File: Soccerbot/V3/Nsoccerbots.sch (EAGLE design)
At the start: 67 parts, among them CN2 1X4-CLEANBIG, IC1 LM340S-05, IC2 TB6612FNG, IC4 TB6612FNG, J3 1X5, J4 1X5, Q1 AOD417, SW2 SPST_TACT-EVQQ2, U1 PCA9685, X1 NXT-SOCKET, X2 NXT-SOCKET, X3 NXT-SOCKET, X4 NXT-SOCKET

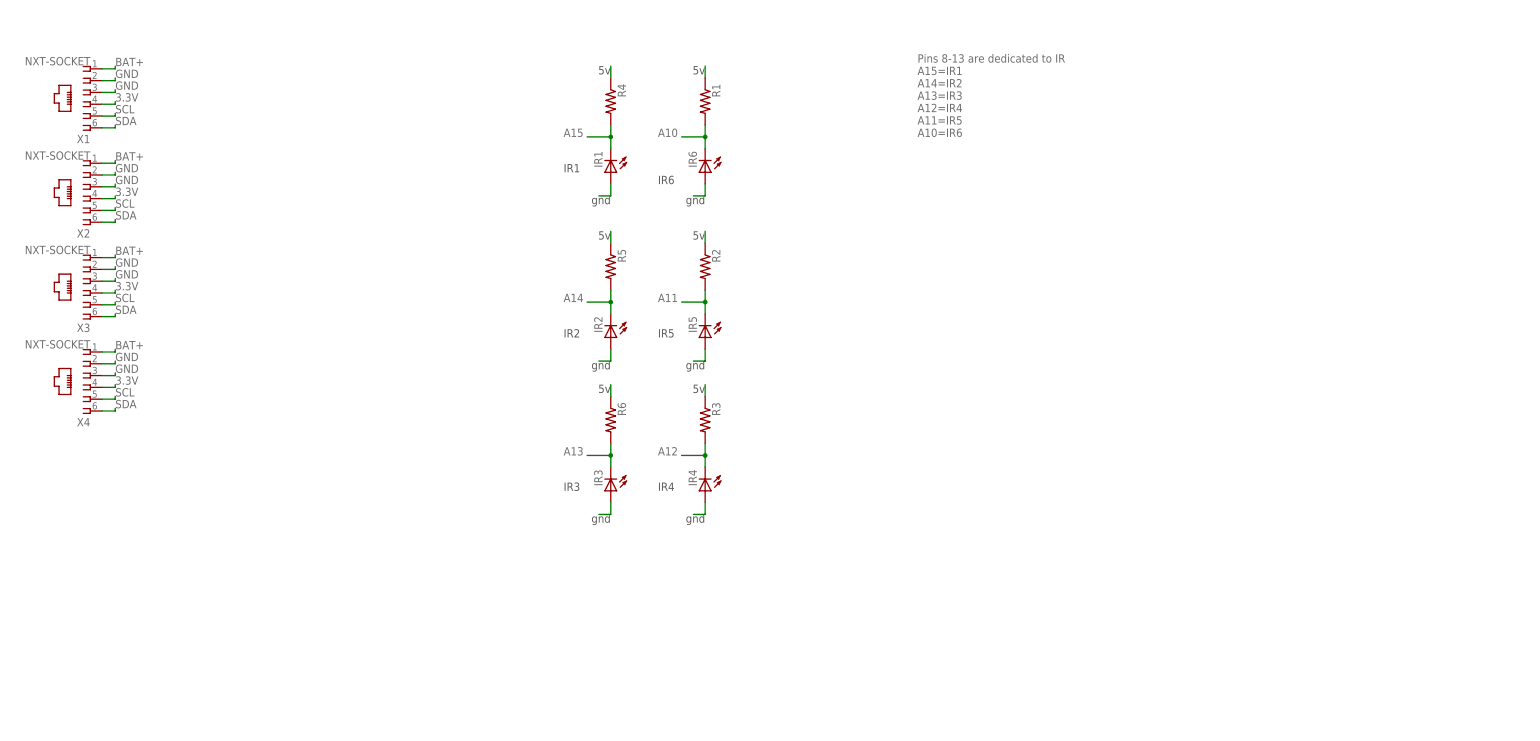
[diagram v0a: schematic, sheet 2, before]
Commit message: Fully routed and all parts in
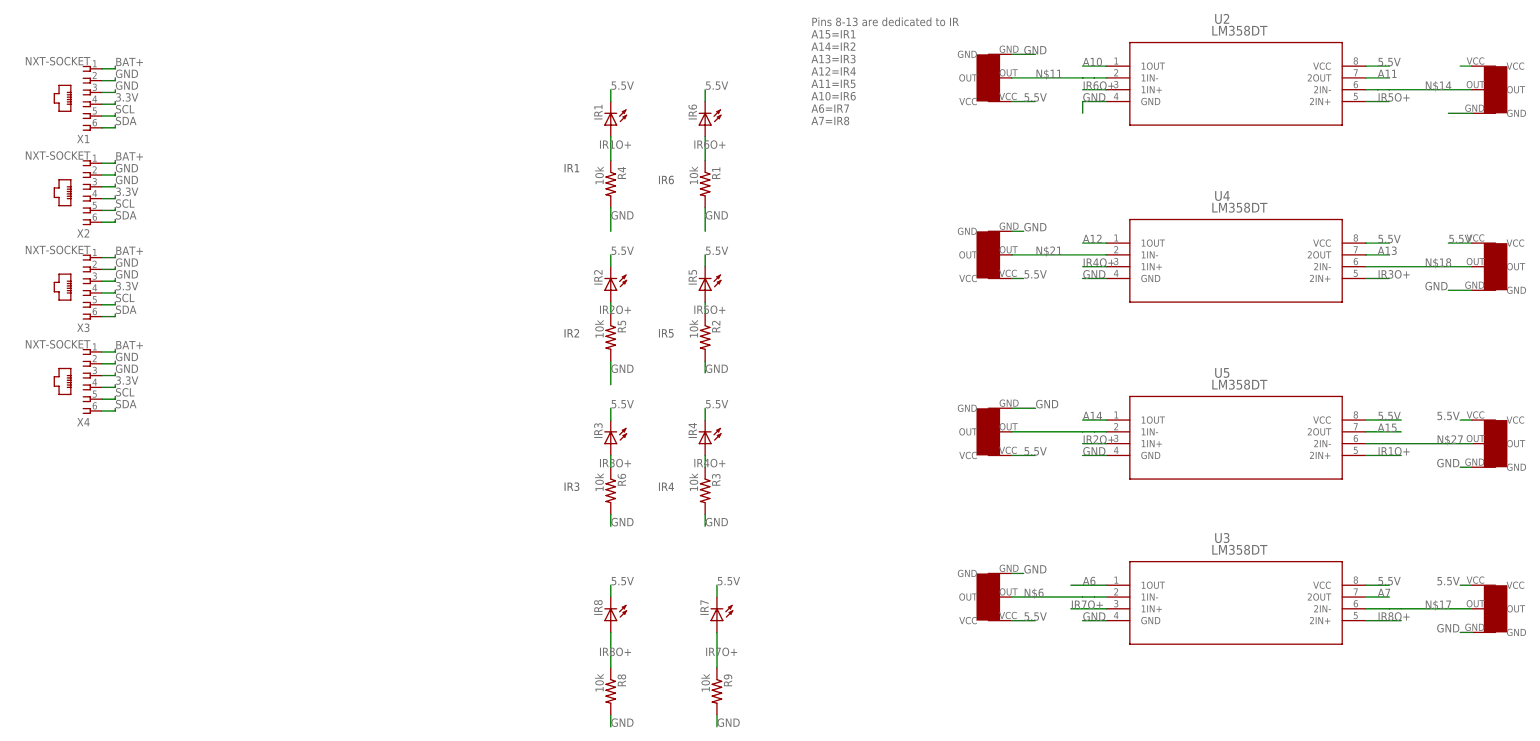
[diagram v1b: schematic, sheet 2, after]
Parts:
- removed R18: 1K, microbuilder:RESISTOR0805_NOOUTLINE
- added IR7, IR8: (no value), led:LED5MM
- added IRP1, IRP2, IRP3, IRP4, IRP5, IRP6, IRP7, IRP8: TRIMPOT, trimPot:TRIMPOT
- added R7: 300ohm, rcl:R-US_R0603
- added R8, R9: 10k, adafruit:R-US_R0603
- added U2, U3, U4, U5: LM358DT, LM358DT:LM358DT
- R1, R2, R3, R4, R5, R6: value (none) -> 10k
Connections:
- removed net GND1: IR5.A
- removed net GND2: IR4.A
- removed net GND3: IR1.A
- removed net GND4: IR2.A
- removed net GND5: IR3.A
- new net IR1O+: IR1.A, R4.1, U5.2IN+
- new net IR2O+: IR2.A, R5.1, U5.1IN+
- new net IR3O+: IR3.A, R6.1, U4.2IN+
- new net IR4O+: IR4.A, R3.1, U4.1IN+
- new net IR5O+: IR5.A, R2.1, U2.2IN+
- new net IR6O+: IR6.A, R1.1, U2.1IN+
- new net IR7O+: IR7.A, R9.1, U3.1IN+
- new net IR8O+: IR8.A, R8.1, U3.2IN+
- new net N$11: IRP6.OUT, U2.1IN-
- new net N$14: IRP5.OUT, U2.2IN-
- new net N$17: IRP8.OUT, U3.2IN-
- new net N$18: IRP3.OUT, U4.2IN-
- new net N$21: IRP4.OUT, U4.1IN-
- new net N$24: IRP2.OUT, U5.1IN-
- new net N$27: IRP1.OUT, U5.2IN-
- new net N$6: IRP7.OUT, U3.1IN-
- net 5.5V: now also IR1.C, IR2.C, IR3.C, IR4.C, IR5.C, IR6.C, IR7.C, IR8.C, IRP1.VCC, IRP2.VCC, IRP3.VCC, IRP4.VCC, IRP5.VCC, IRP6.VCC, IRP7.VCC, IRP8.VCC, LED2.A, U2.VCC, U3.VCC, U4.VCC, U5.VCC; no longer R1.1, R2.1, R3.1, R4.1, R5.1, R6.1
- net A10: now also U2.1OUT; no longer IR6.C, R1.2
- net A11: now also U2.2OUT; no longer IR5.C, R2.2
- net A12: now also U4.1OUT; no longer IR4.C, R3.2
- net A13: now also U4.2OUT; no longer IR3.C, R6.2
- net A14: now also U5.1OUT; no longer IR2.C, R5.2
- net A15: now also U5.2OUT; no longer IR1.C, R4.2
- net A6: now also U3.1OUT
- net A7: now also U3.2OUT
- net BAT+: no longer LED2.A
- net GND: now also IRP1.GND, IRP2.GND, IRP3.GND, IRP4.GND, IRP5.GND, IRP6.GND, IRP7.GND, IRP8.GND, R1.2, R2.2, R3.2, R4.2, R5.2, R6.2, R7.1, R8.2, R9.2, U2.GND, U3.GND, U4.GND, U5.GND; no longer IR6.A, R18.1
- net N$1: now also R7.2; no longer R18.2
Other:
- note added: "Pins 8-13 are dedicated to IR A15=IR1 A14=IR2 A13=IR3 A12=IR4 A11=IR5 A10=IR6 A6=IR7 A7=IR8"
- note removed: "5v"
- note removed: "gnd"
- moved on the sheet: IR1, IR2, IR3, IR4, IR5, IR6, R1, R2, R3, R4, R5, R6

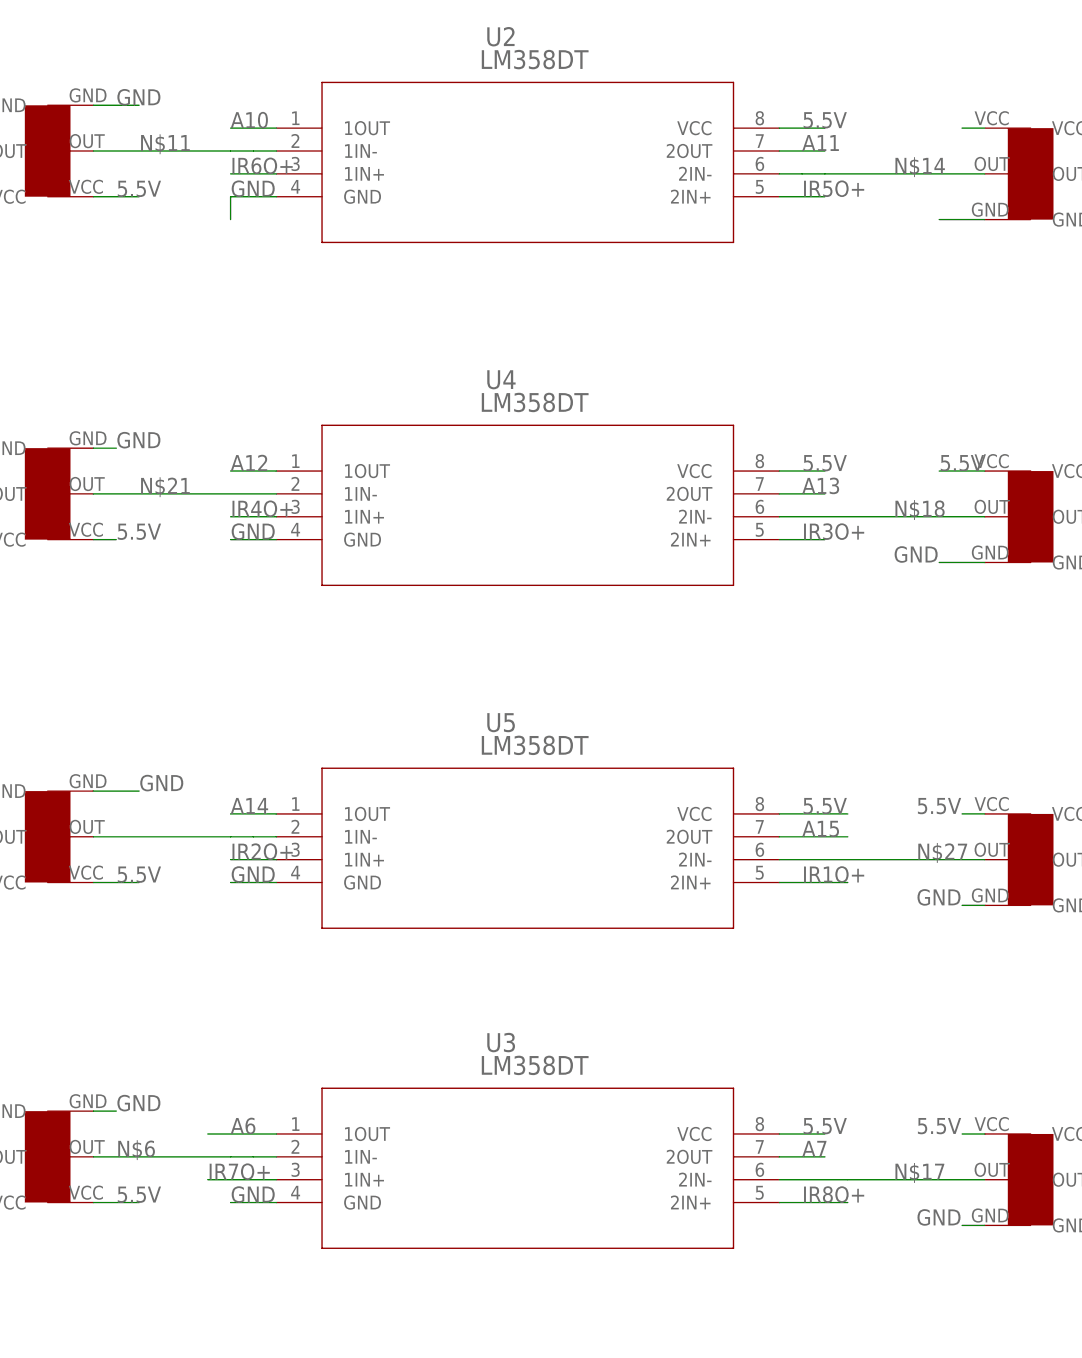
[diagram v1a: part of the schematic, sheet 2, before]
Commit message: added resistors
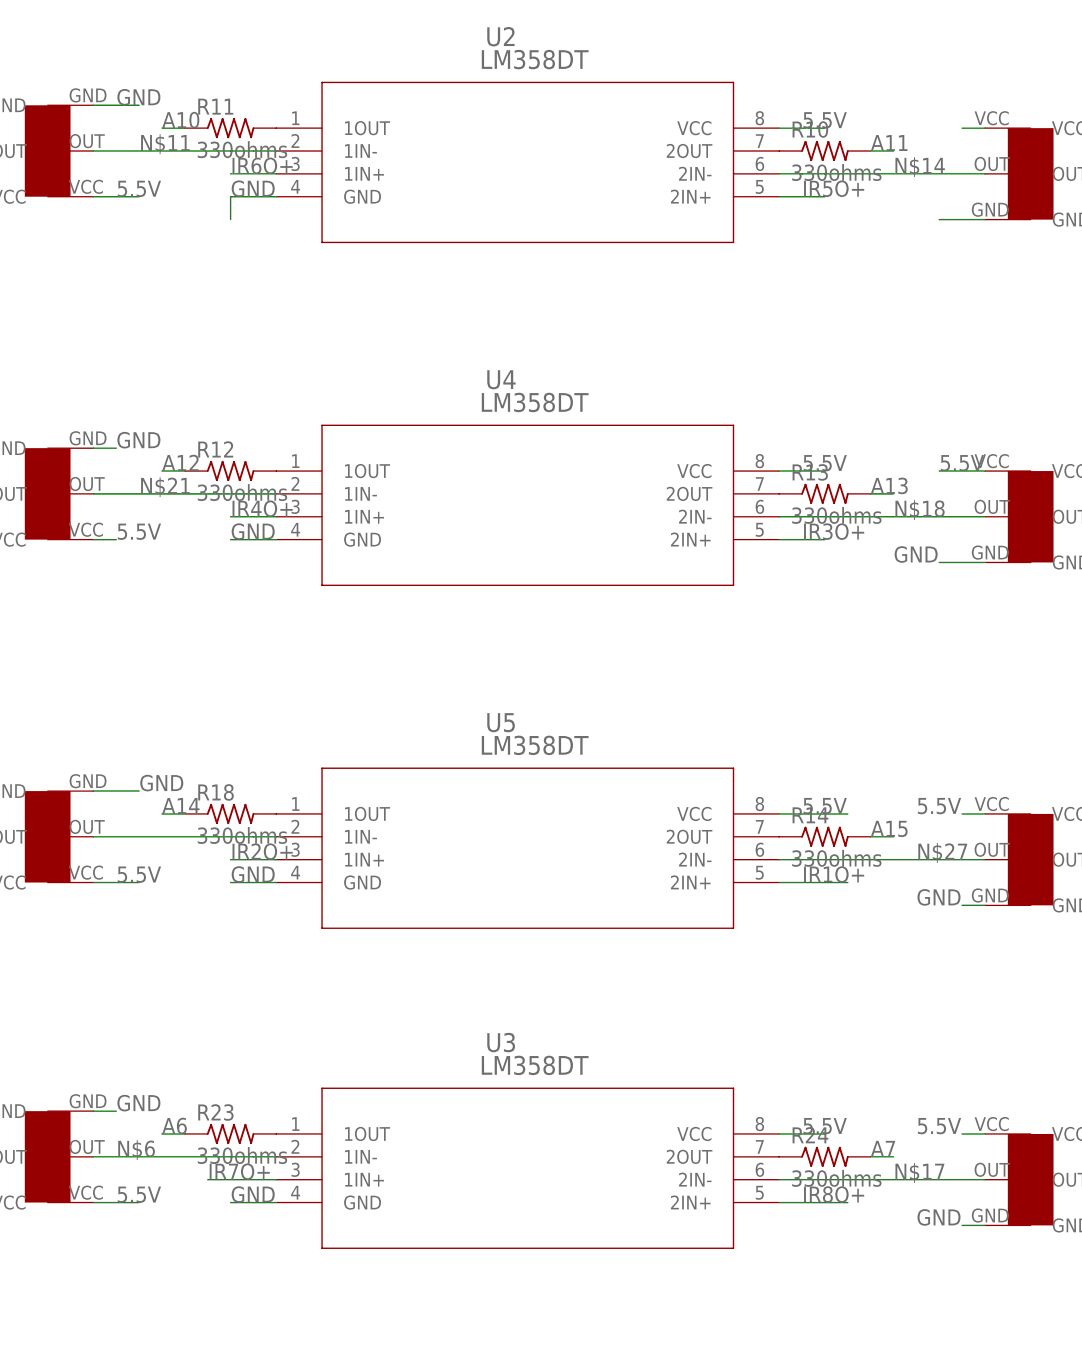
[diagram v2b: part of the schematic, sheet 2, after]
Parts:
- added R10, R11, R12, R13, R14, R18, R23, R24: 330ohms, resistor:R-US_R0603
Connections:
- new net N$10: R14.1, U5.2OUT
- new net N$12: R18.2, U5.1OUT
- new net N$13: R23.2, U3.1OUT
- new net N$15: R24.1, U3.2OUT
- new net N$2: R10.1, U2.2OUT
- new net N$7: R11.2, U2.1OUT
- new net N$8: R12.2, U4.1OUT
- new net N$9: R13.1, U4.2OUT
- net A10: now also R11.1; no longer U2.1OUT
- net A11: now also R10.2; no longer U2.2OUT
- net A12: now also R12.1; no longer U4.1OUT
- net A13: now also R13.2; no longer U4.2OUT
- net A14: now also R18.1; no longer U5.1OUT
- net A15: now also R14.2; no longer U5.2OUT
- net A6: now also R23.1; no longer U3.1OUT
- net A7: now also R24.2; no longer U3.2OUT
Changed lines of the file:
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@@
 <part name="IRP1" library="trimPot" deviceset="TRIMPOT" device=""/>
 <part name="IRP8" library="trimPot" deviceset="TRIMPOT" device=""/>
+<part name="R10" library="resistor" library_urn="urn:adsk.eagle:library:348" deviceset="R-US_" device="R0603" package3d_urn="urn:adsk.eagle:package:26057/1" value="330ohms"/>
+<part name="R11" library="resistor" library_urn="urn:adsk.eagle:library:348" deviceset="R-US_" device="R0603" package3d_urn="urn:adsk.eagle:package:26057/1" value="330ohms"/>
+<part name="R12" library="resistor" library_urn="urn:adsk.eagle:library:348" deviceset="R-US_" device="R0603" package3d_urn="urn:adsk.eagle:package:26057/1" value="330ohms"/>
+<part name="R13" library="resistor" library_urn="urn:adsk.eagle:library:348" deviceset="R-US_" device="R0603" package3d_urn="urn:adsk.eagle:package:26057/1" value="330ohms"/>
+<part name="R14" library="resistor" library_urn="urn:adsk.eagle:library:348" deviceset="R-US_" device="R0603" package3d_urn="urn:adsk.eagle:package:26057/1" value="330ohms"/>
+<part name="R18" library="resistor" library_urn="urn:adsk.eagle:library:348" deviceset="R-US_" device="R0603" package3d_urn="urn:adsk.eagle:package:26057/1" value="330ohms"/>
+<part name="R23" library="resistor" library_urn="urn:adsk.eagle:library:348" deviceset="R-US_" device="R0603" package3d_urn="urn:adsk.eagle:package:26057/1" value="330ohms"/>
+<part name="R24" library="resistor" library_urn="urn:adsk.eagle:library:348" deviceset="R-US_" device="R0603" package3d_urn="urn:adsk.eagle:package:26057/1" value="330ohms"/>
 </parts>
 <sheets>
@@
 <instance part="IRP1" gate="G$1" x="378.46" y="-58.42"/>
 <instance part="IRP8" gate="G$1" x="378.46" y="-93.98"/>
+<instance part="R10" gate="G$1" x="355.6" y="20.32"/>
+<instance part="R11" gate="G$1" x="289.56" y="22.86"/>
+<instance part="R12" gate="G$1" x="289.56" y="-15.24"/>
+<instance part="R13" gate="G$1" x="355.6" y="-17.78"/>
+<instance part="R14" gate="G$1" x="355.6" y="-55.88"/>
+<instance part="R18" gate="G$1" x="289.56" y="-53.34"/>
+<instance part="R23" gate="G$1" x="289.56" y="-88.9"/>
+<instance part="R24" gate="G$1" x="355.6" y="-91.44"/>
 </instances>
 <busses>
@@
 </segment>
 </net>
-<net name="A11" class="0">
-<segment>
-<pinref part="U2" gate="A" pin="2OUT"/>
-<wire x1="350.52" y1="20.32" x2="355.6" y2="20.32" width="0.1524" layer="91"/>
-<label x="353.06" y="20.32" size="1.778" layer="95"/>
-</segment>
-</net>
 <net name="N$14" class="0">
 <segment>
@@
 </segment>
 </net>
-<net name="A10" class="0">
-<segment>
-<pinref part="U2" gate="A" pin="1OUT"/>
-<wire x1="294.64" y1="22.86" x2="289.56" y2="22.86" width="0.1524" layer="91"/>
-<label x="289.56" y="22.86" size="1.778" layer="95"/>
-</segment>
-</net>
-<net name="A13" class="0">
-<segment>
-<pinref part="U4" gate="A" pin="2OUT"/>
-<wire x1="350.52" y1="-17.78" x2="355.6" y2="-17.78" width="0.1524" layer="91"/>
-<label x="353.06" y="-17.78" size="1.778" layer="95"/>
-</segment>
-</net>
 <net name="N$18" class="0">
 <segment>
@@
 <wire x1="274.32" y1="-17.78" x2="294.64" y2="-17.78" width="0.1524" layer="91"/>
 <label x="279.4" y="-17.78" size="1.778" layer="95"/>
-</segment>
-</net>
-<net name="A12" class="0">
-<segment>
-<pinref part="U4" gate="A" pin="1OUT"/>
-<wire x1="294.64" y1="-15.24" x2="289.56" y2="-15.24" width="0.1524" layer="91"/>
-<label x="289.56" y="-15.24" size="1.778" layer="95"/>
-</segment>
-</net>
-<net name="A14" class="0">
-<segment>
-<pinref part="U5" gate="A" pin="1OUT"/>
-<wire x1="294.64" y1="-53.34" x2="289.56" y2="-53.34" width="0.1524" layer="91"/>
-<label x="289.56" y="-53.34" size="1.778" layer="95"/>
 </segment>
 </net>
@@
 </segment>
 </net>
-<net name="A15" class="0">
-<segment>
-<pinref part="U5" gate="A" pin="2OUT"/>
-<wire x1="350.52" y1="-55.88" x2="358.14" y2="-55.88" width="0.1524" layer="91"/>
-<label x="353.06" y="-55.88" size="1.778" layer="95"/>
-</segment>
-</net>
 <net name="N$27" class="0">
 <segment>
@@
 <wire x1="294.64" y1="-93.98" x2="287.02" y2="-93.98" width="0.1524" layer="91"/>
 <label x="287.02" y="-93.98" size="1.778" layer="95"/>
-</segment>
-</net>
-<net name="A6" class="0">
-<segment>
-<pinref part="U3" gate="A" pin="1OUT"/>
-<wire x1="294.64" y1="-88.9" x2="287.02" y2="-88.9" width="0.1524" layer="91"/>
-<label x="289.56" y="-88.9" size="1.778" layer="95"/>
 </segment>
 </net>
@@
 </segment>
 </net>
-<net name="A7" class="0">
-<segment>
-<pinref part="U3" gate="A" pin="2OUT"/>
-<wire x1="350.52" y1="-91.44" x2="355.6" y2="-91.44" width="0.1524" layer="91"/>
-<label x="353.06" y="-91.44" size="1.778" layer="95"/>
-</segment>
-</net>
 <net name="N$17" class="0">
 <segment>
@@
 </segment>
 </net>
+<net name="N$2" class="0">
+<segment>
+<pinref part="U2" gate="A" pin="2OUT"/>
+<pinref part="R10" gate="G$1" pin="1"/>
+</segment>
+</net>
+<net name="N$7" class="0">
+<segment>
+<pinref part="U2" gate="A" pin="1OUT"/>
+<pinref part="R11" gate="G$1" pin="2"/>
+</segment>
+</net>
+<net name="N$8" class="0">
+<segment>
+<pinref part="U4" gate="A" pin="1OUT"/>
+<pinref part="R12" gate="G$1" pin="2"/>
+</segment>
+</net>
+<net name="N$9" class="0">
+<segment>
+<pinref part="U4" gate="A" pin="2OUT"/>
+<pinref part="R13" gate="G$1" pin="1"/>
+</segment>
+</net>
+<net name="N$10" class="0">
+<segment>
+<pinref part="U5" gate="A" pin="2OUT"/>
+<pinref part="R14" gate="G$1" pin="1"/>
+</segment>
+</net>
+<net name="N$12" class="0">
+<segment>
+<pinref part="U5" gate="A" pin="1OUT"/>
+<pinref part="R18" gate="G$1" pin="2"/>
+</segment>
+</net>
+<net name="N$13" class="0">
+<segment>
+<pinref part="U3" gate="A" pin="1OUT"/>
+<pinref part="R23" gate="G$1" pin="2"/>
+</segment>
+</net>
+<net name="N$15" class="0">
+<segment>
+<pinref part="U3" gate="A" pin="2OUT"/>
+<pinref part="R24" gate="G$1" pin="1"/>
+</segment>
+</net>
+<net name="A6" class="0">
+<segment>
+<pinref part="R23" gate="G$1" pin="1"/>
+<wire x1="284.48" y1="-88.9" x2="281.94" y2="-88.9" width="0.1524" layer="91"/>
+<label x="281.94" y="-88.9" size="1.778" layer="95"/>
+</segment>
+</net>
+<net name="A7" class="0">
+<segment>
+<pinref part="R24" gate="G$1" pin="2"/>
+<wire x1="360.68" y1="-91.44" x2="363.22" y2="-91.44" width="0.1524" layer="91"/>
+<label x="360.68" y="-91.44" size="1.778" layer="95"/>
+</segment>
+</net>
+<net name="A15" class="0">
+<segment>
+<pinref part="R14" gate="G$1" pin="2"/>
+<wire x1="360.68" y1="-55.88" x2="363.22" y2="-55.88" width="0.1524" layer="91"/>
+<label x="360.68" y="-55.88" size="1.778" layer="95"/>
+</segment>
+</net>
+<net name="A14" class="0">
+<segment>
+<pinref part="R18" gate="G$1" pin="1"/>
+<wire x1="284.48" y1="-53.34" x2="281.94" y2="-53.34" width="0.1524" layer="91"/>
+<label x="281.94" y="-53.34" size="1.778" layer="95"/>
+</segment>
+</net>
+<net name="A12" class="0">
+<segment>
+<pinref part="R12" gate="G$1" pin="1"/>
+<wire x1="284.48" y1="-15.24" x2="281.94" y2="-15.24" width="0.1524" layer="91"/>
+<label x="281.94" y="-15.24" size="1.778" layer="95"/>
+</segment>
+</net>
+<net name="A13" class="0">
+<segment>
+<pinref part="R13" gate="G$1" pin="2"/>
+<wire x1="360.68" y1="-17.78" x2="363.22" y2="-17.78" width="0.1524" layer="91"/>
+<label x="360.68" y="-17.78" size="1.778" layer="95"/>
+</segment>
+</net>
+<net name="A10" class="0">
+<segment>
+<pinref part="R11" gate="G$1" pin="1"/>
+<wire x1="284.48" y1="22.86" x2="281.94" y2="22.86" width="0.1524" layer="91"/>
+<label x="281.94" y="22.86" size="1.778" layer="95"/>
+</segment>
+</net>
+<net name="A11" class="0">
+<segment>
+<pinref part="R10" gate="G$1" pin="2"/>
+<wire x1="360.68" y1="20.32" x2="363.22" y2="20.32" width="0.1524" layer="91"/>
+<label x="360.68" y="20.32" size="1.778" layer="95"/>
+</segment>
+</net>

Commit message: x
x
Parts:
- C14: MPN EEFCX0J101R -> ERJ-3EKF1270V; OC_NEWARK 17AC6838 -> 53W4521
- IC1: MPN (none) -> LM1085ISX-5.0/NOPB; OC_NEWARK (none) -> 01AC5221
- IRP1, IRP2, IRP3, IRP4, IRP5, IRP6, IRP7, IRP8: MPN (none) -> TC33X-2-103E; OC_NEWARK (none) -> 97M3836
- Q1: MPN (none) -> AUIRFR540ZTRL; OC_NEWARK (none) -> 91Y4154
- R10, R11, R12, R13, R14, R18, R23, R24: MPN (none) -> CRCW060310K0FKEAHP; OC_NEWARK (none) -> 68R2991
- R7: OC_NEWARK (none) -> unknown
- U2, U3, U4, U5: MPN (none) -> LM258DT; OC_NEWARK (none) -> 22AC3037
